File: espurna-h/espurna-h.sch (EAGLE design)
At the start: 51 parts, among them IC1 AMS1117-3.3, IC2 ESP-12-SMD, IC3 PC817CS, IC4 HLW8012

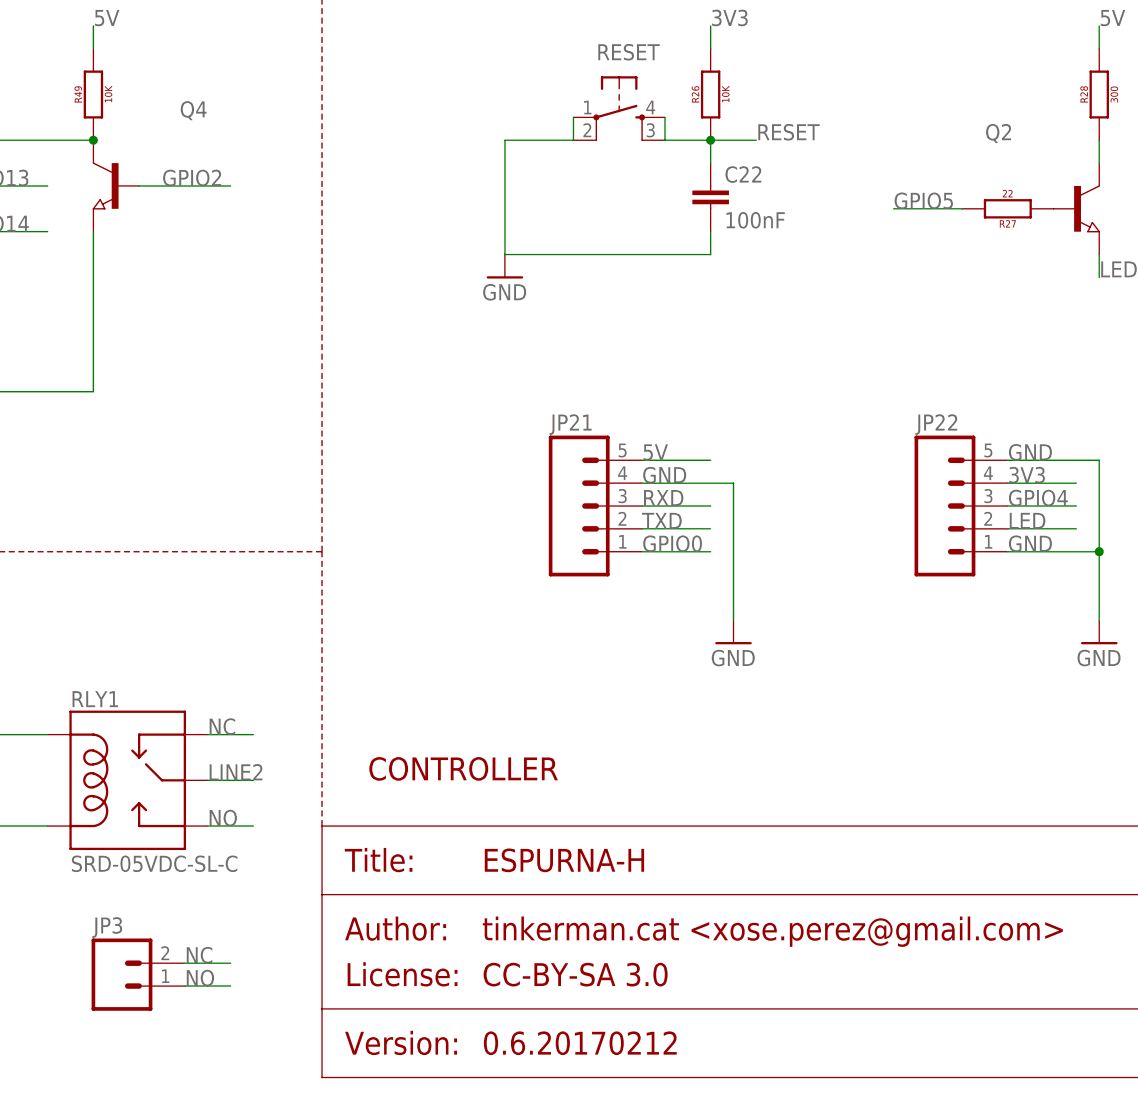
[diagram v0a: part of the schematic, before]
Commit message: Swapped GPIO2 and GPIO5 to avoid the module LED to change with HLW8012 SEL pin value
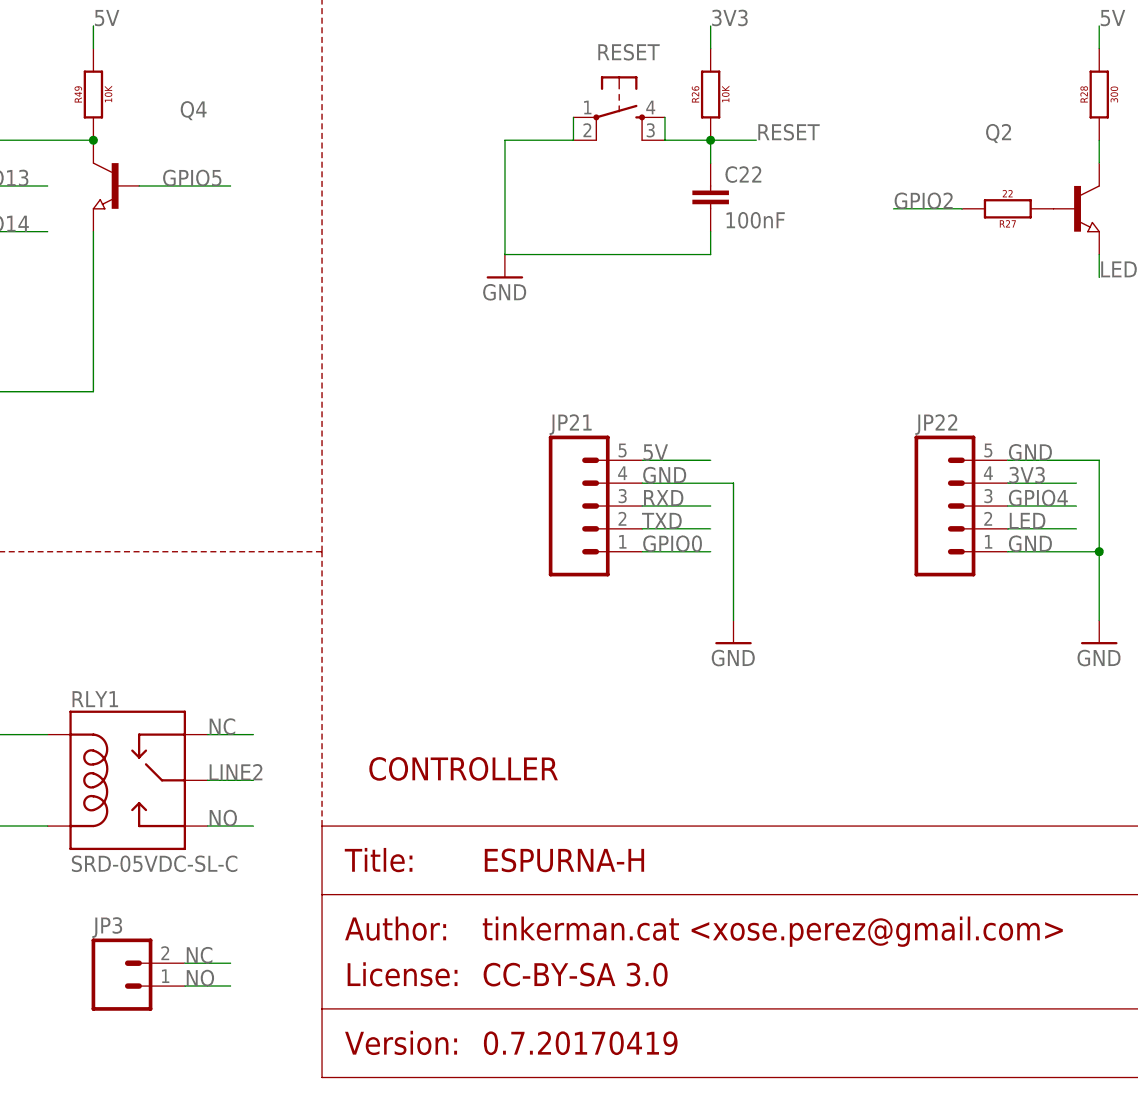
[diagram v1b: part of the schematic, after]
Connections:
- net GPIO2: now also R27.2; no longer Q4.B
- net GPIO5: now also Q4.B; no longer R27.2
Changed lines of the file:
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@@
 <attribute name="PROJECT_LICENSE" value="CC-BY-SA 3.0"/>
 <attribute name="PROJECT_NAME" value="ESPURNA-H"/>
-<attribute name="PROJECT_VERSION" value="0.6.20170212"/>
+<attribute name="PROJECT_VERSION" value="0.7.20170419"/>
 </attributes>
 <variantdefs>
@@
 </segment>
 <segment>
-<pinref part="R27" gate="G$1" pin="2"/>
-<wire x1="233.68" y1="96.52" x2="226.06" y2="96.52" width="0.1524" layer="91"/>
-<label x="226.06" y="96.52" size="1.778" layer="95"/>
+<pinref part="Q4" gate="G$1" pin="B"/>
+<wire x1="142.24" y1="99.06" x2="152.4" y2="99.06" width="0.1524" layer="91"/>
+<label x="144.78" y="99.06" size="1.778" layer="95"/>
 </segment>
 </net>
@@
 </segment>
 <segment>
-<pinref part="Q4" gate="G$1" pin="B"/>
-<wire x1="142.24" y1="99.06" x2="152.4" y2="99.06" width="0.1524" layer="91"/>
-<label x="144.78" y="99.06" size="1.778" layer="95"/>
-</segment>
-</net>
+<pinref part="R27" gate="G$1" pin="2"/>
+<wire x1="233.68" y1="96.52" x2="226.06" y2="96.52" width="0.1524" layer="91"/>
+<label x="226.06" y="96.52" size="1.778" layer="95"/>
+</segment>
+</net>

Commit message: Change varistor symbol, added thermal fuse, change measurement point
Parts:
- removed FUSE: FUSEX20MM, xose:FUSEX20MM
- removed IC3: PC817CS, optocoupler:SFH6186-2
- removed VARISTOR: V18ZA2P, SparkFun-DiscreteSemi:V18ZA2P
- added F1: 73C, fuse:PICOFUSE
- added F2: FUSEX20MM, xose:FUSEX20MM
- added R11: S10K250, varistor:S10K250
- Q3: device xose:NPN-TRANSISTOR_SOT23 -> xose:MOSFET-N
- R31: value 220 -> 1K
- R32: value 1K -> 10K
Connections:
- removed net N$15: IC3.C, R31.1
- removed net N$6: IC3.EMIT, R32.1
- removed net N$8: FUSE.2, U$1.AC_L, VARISTOR.P$2
- new net LINE3: R1.1, R42.2, R44.2, RLY1.MAIN
- new net N$7: F1.2, F2.1
- net 3V3: no longer IC3.A
- net 5V: no longer IC3.COL
- net GND: now also Q3.S, R32.1; no longer Q3.E
- net GPIO12: now also R31.1; no longer R31.2
- net LINE1: now also F1.1; no longer FUSE.1, R1.2, R43.2
- net LINE2: now also F2.2, R1.2, R11.2, R43.2, U$1.AC_L; no longer R1.1, R42.2, R44.2, RLY1.MAIN
- net N$4: now also Q3.D; no longer Q3.C
- net N$5: now also Q3.G, R31.2; no longer Q3.B
- net NEUTRAL: now also R11.1; no longer VARISTOR.P$1
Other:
- moved on the sheet: D3, JP3, R31, R32, RLY1

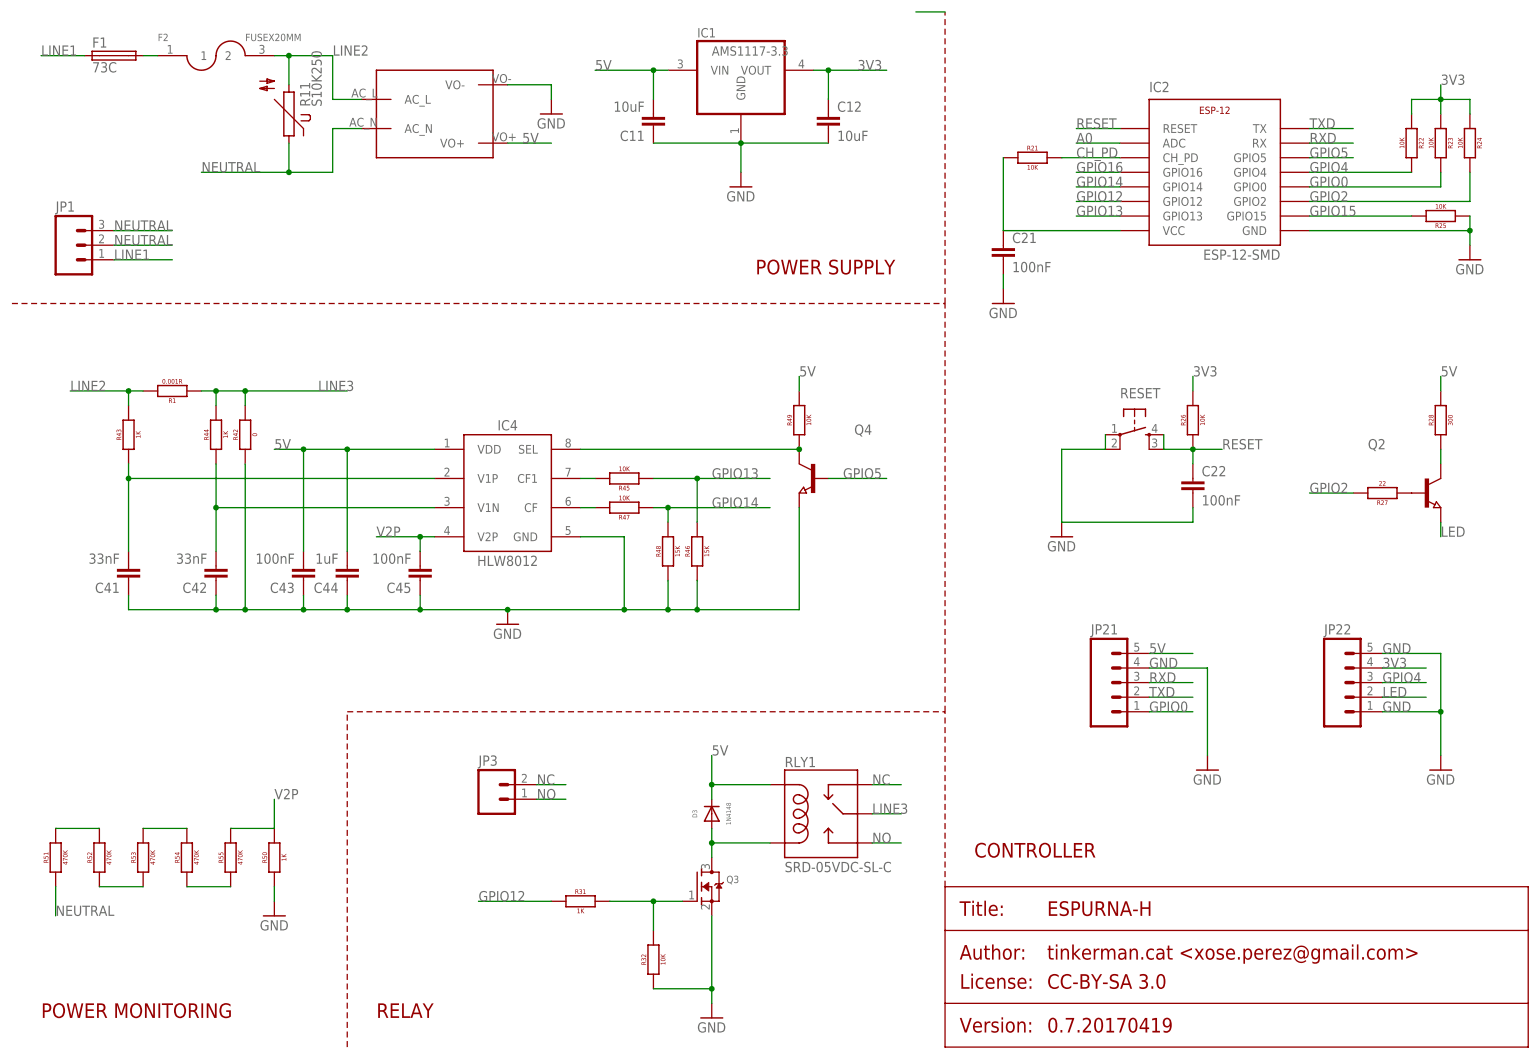
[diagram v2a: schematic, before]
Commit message: Separate power from load. Wire
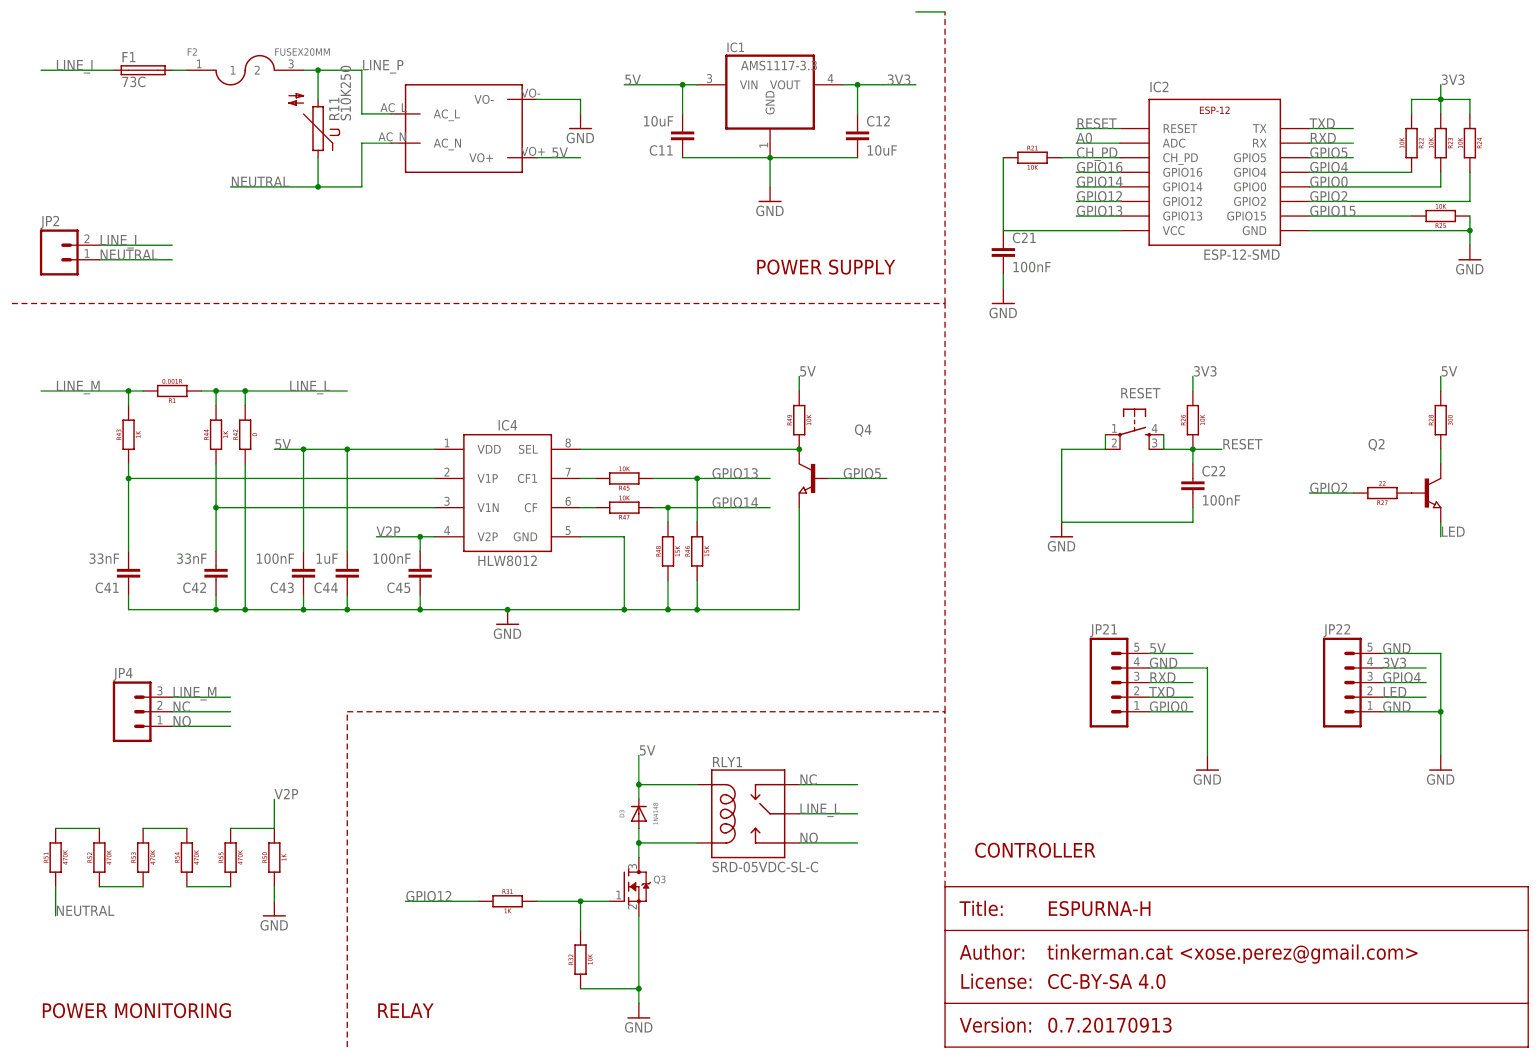
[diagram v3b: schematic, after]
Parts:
- removed JP1: (no value), xose:M03200MIL
- removed JP3: (no value), xose:M02200MIL
- added JP2: (no value), xose:M02200MIL
- added JP4: (no value), xose:M03200MIL
- Q3: device xose:MOSFET-N -> xose:MOSFET-NREFLOW
- R11: device varistor:S10K250 -> xose:S10K250
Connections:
- net LINE3 renamed LINE_L
- removed net LINE1: F1.1, JP1.1
- removed net LINE2: F2.2, R1.2, R11.2, R43.2, U$1.AC_L
- new net LINE_I: F1.1, JP2.2
- new net LINE_M: JP4.3, R1.2, R43.2
- new net LINE_P: F2.2, R11.2, U$1.AC_L
- net NC: now also JP4.2; no longer JP3.2
- net NEUTRAL: now also JP2.1; no longer JP1.2, JP1.3
- net NO: now also JP4.1; no longer JP3.1
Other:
- moved on the sheet: C11, C12, D3, F1, F2, IC1, Q3, R11, R31, R32, RLY1

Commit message: Version 0.7.20170913
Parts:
- added V11: S10K250, xose:S10K250
- R11: value S10K250 -> 0R; device xose:S10K250 -> xose:RESISTOR1206
- R42: value 0 -> 0R
- renumbered R1 to R41
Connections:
- removed net N$18: R52.1, R53.1
- removed net N$19: R51.2, R52.2
- new net N$15: R51.1, R52.2
- new net N$16: R52.1, R53.2
- net LINE_I: now also R11.2
- net LINE_M: now also R51.2
- net LINE_P: now also R11.1, V11.2; no longer R11.2
- net N$17: now also R53.1; no longer R53.2
- net NEUTRAL: now also V11.1; no longer R11.1, R51.1
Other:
- moved on the sheet: R51, R53
